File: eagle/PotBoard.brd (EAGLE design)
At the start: 62 x 29 mm, 29 parts, among them IC1 MEGA8-AI, Q1 20MHz, Q3 IRLML5203, X1 MICROMATCH-8SMD

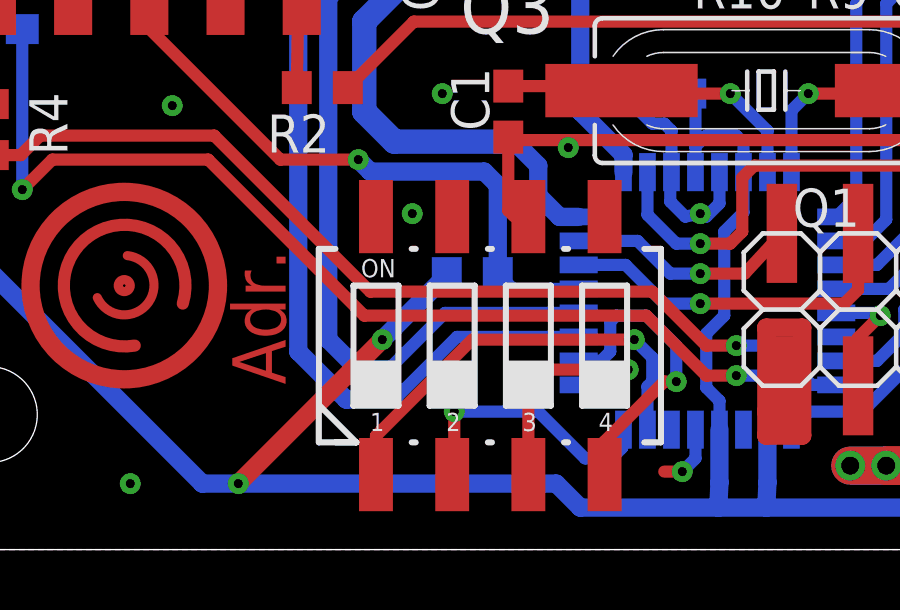
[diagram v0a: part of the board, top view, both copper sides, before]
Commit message: Removed a stupid error from the pcbs and included an instructions file. Switched the firmware to use just two switches instead of four. No one's gonna build an arc16 anyway.
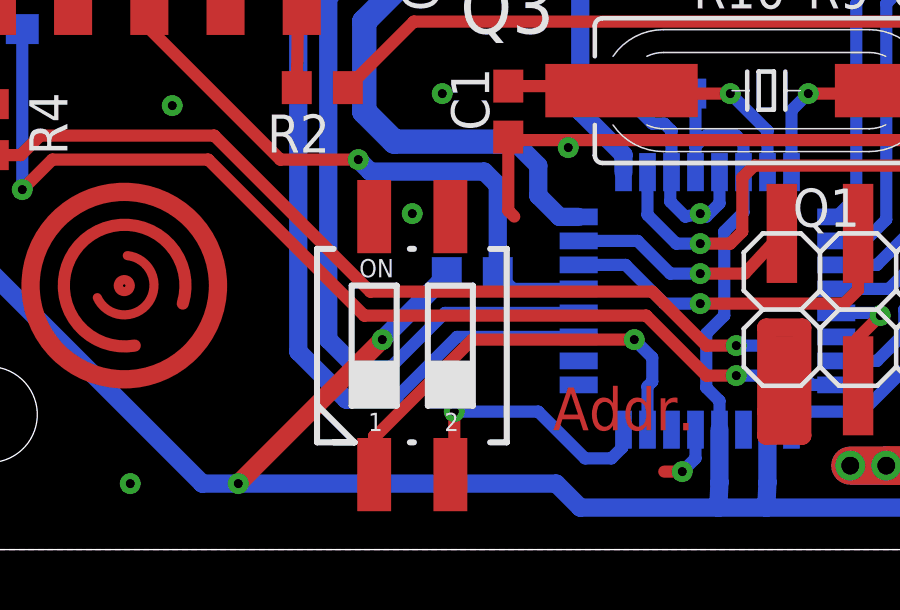
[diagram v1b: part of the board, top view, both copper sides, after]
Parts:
- removed S1: 219-04, switch-dil:CTS-219-04
- added ADRESS: 219-02, switch-dil:CTS-219-02
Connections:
- removed net N$22: IC1.25, S1.3
- removed net N$23: IC1.26, S1.4
- net GND: now also ADRESS.3, ADRESS.4; no longer S1.5, S1.6, S1.7, S1.8
- net N$20: now also ADRESS.2; no longer S1.2
- net N$6: now also ADRESS.1; no longer S1.1
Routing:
- net N$23: track 10.4 -> 0.00 mm, vias 1 -> 0
- net N$22: track 8.27 -> 0.00 mm, vias 1 -> 0
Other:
- board text added: "Addr."
- board text removed: "Adr."
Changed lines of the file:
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@@
 <layer number="17" name="Pads" color="2" fill="1" visible="yes" active="yes"/>
 <layer number="18" name="Vias" color="2" fill="1" visible="yes" active="yes"/>
-<layer number="19" name="Unrouted" color="6" fill="1" visible="no" active="yes"/>
+<layer number="19" name="Unrouted" color="6" fill="1" visible="yes" active="yes"/>
 <layer number="20" name="Dimension" color="15" fill="1" visible="yes" active="yes"/>
 <layer number="21" name="tPlace" color="7" fill="1" visible="yes" active="yes"/>
 <layer number="22" name="bPlace" color="7" fill="1" visible="no" active="yes"/>
-<layer number="23" name="tOrigins" color="15" fill="1" visible="no" active="yes"/>
+<layer number="23" name="tOrigins" color="15" fill="1" visible="yes" active="yes"/>
 <layer number="24" name="bOrigins" color="15" fill="1" visible="no" active="yes"/>
 <layer number="25" name="tNames" color="7" fill="1" visible="yes" active="yes"/>
@@
 <circle x="9" y="8.8" radius="0.2" width="0.3048" layer="1"/>
 <text x="60.6" y="7" size="2.54" layer="1" font="vector" ratio="16" rot="R90">Arc_Base</text>
-<text x="12.6" y="10" size="1.778" layer="1" font="vector" ratio="15" rot="R270">Adr.</text>
+<text x="28" y="5.4" size="1.4224" layer="1" font="vector" ratio="15" rot="R180">Addr.</text>
 <text x="42.2" y="26.6" size="1.27" layer="1" font="vector" ratio="17">Johannes Neumann</text>
 <text x="61" y="25.2" size="2.54" layer="16" font="vector" ratio="16" rot="MR270">Arc_Base</text>
@@
 <attribute name="VALUE" x="29.65" y="3.555" size="1.27" layer="27"/>
 </element>
-<element name="S1" library="switch-dil" package="CTS-219-04" value="219-04" x="21.2" y="6.8" smashed="yes">
-<attribute name="OC_NEWARK" value="unknown" x="21.2" y="6.8" size="1.27" layer="27" font="vector" ratio="17" display="off"/>
-<attribute name="MPN" value="" x="21.2" y="6.8" size="1.27" layer="27" font="vector" ratio="17" display="off"/>
-<attribute name="MF" value="" x="21.2" y="6.8" size="1.27" layer="27" font="vector" ratio="17" display="off"/>
-<attribute name="OC_FARNELL" value="unknown" x="21.2" y="6.8" size="1.27" layer="27" font="vector" ratio="17" display="off"/>
-</element>
 <element name="R2" library="rcl" package="R0603" value="330" x="15.6" y="15.4" smashed="yes">
 <attribute name="NAME" x="13.765" y="13.235" size="1.27" layer="25"/>
@@
 <element name="X1" library="con-amp-micromatch-2" package="MICROMATCH-8-SMD" value="MICROMATCH-8SMD" x="49.4" y="21.6" smashed="yes" rot="R180">
 <attribute name="NAME" x="55.045" y="18.66" size="1.27" layer="25" rot="R180"/>
+</element>
+<element name="ADRESS" library="switch-dil" package="CTS-219-02" value="219-02" x="18.6" y="6.8" smashed="yes">
+<attribute name="OC_NEWARK" value="unknown" x="18.6" y="6.8" size="1.778" layer="27" display="off"/>
+<attribute name="MPN" value="" x="18.6" y="6.8" size="1.778" layer="27" display="off"/>
+<attribute name="MF" value="" x="18.6" y="6.8" size="1.778" layer="27" display="off"/>
+<attribute name="OC_FARNELL" value="unknown" x="18.6" y="6.8" size="1.778" layer="27" display="off"/>
 </element>
 </elements>
@@
 <via x="2.4" y="8.8" extent="1-16" drill="0.3" shape="octagon"/>
 <via x="39.8" y="7.8" extent="1-16" drill="0.3" shape="octagon"/>
-<contactref element="S1" pad="5"/>
-<contactref element="S1" pad="6"/>
-<contactref element="S1" pad="7"/>
-<contactref element="S1" pad="8"/>
 <via x="38.6" y="25.8" extent="1-16" drill="0.3" shape="octagon"/>
 <via x="49.6" y="12.8" extent="1-16" drill="0.3" shape="octagon"/>
@@
 <wire x1="30.92" y1="5.46" x2="30.92" y2="5.12" width="0.6096" layer="1"/>
 <wire x1="30.92" y1="5.12" x2="30.4" y2="4.6" width="0.6096" layer="1"/>
+<contactref element="ADRESS" pad="3"/>
+<contactref element="ADRESS" pad="4"/>
 </signal>
 <signal name="VCC">
@@
 <wire x1="26.6" y1="6.4" x2="26" y2="7" width="0.4064" layer="16"/>
 <wire x1="26" y1="7" x2="20.6" y2="7" width="0.4064" layer="1"/>
-<contactref element="S1" pad="1"/>
-<wire x1="17.39" y1="2.5" x2="17.39" y2="3.79" width="0.4064" layer="1"/>
+<contactref element="ADRESS" pad="1"/>
+<wire x1="17.39" y1="3.79" x2="17.33" y2="3.79" width="0.4064" layer="1"/>
+<wire x1="17.33" y1="3.79" x2="17.33" y2="2.5" width="0.4064" layer="1"/>
 </signal>
 <signal name="N$20">
@@
 <wire x1="24.36" y1="3.04" x2="22.8" y2="4.6" width="0.4064" layer="16"/>
 <wire x1="22.8" y1="4.6" x2="20" y2="4.6" width="0.4064" layer="16"/>
-<contactref element="S1" pad="2"/>
 <wire x1="20" y1="4.6" x2="20" y2="2.57" width="0.4064" layer="1"/>
-<wire x1="20" y1="2.57" x2="19.93" y2="2.5" width="0.4064" layer="1"/>
-</signal>
-<signal name="N$22">
-<contactref element="IC1" pad="25"/>
-<via x="25.8" y="6" extent="1-16" drill="0.3" shape="octagon"/>
-<wire x1="24.1474" y1="5.49" x2="25.29" y2="5.49" width="0.4064" layer="16"/>
-<wire x1="25.29" y1="5.49" x2="25.8" y2="6" width="0.4064" layer="16"/>
-<contactref element="S1" pad="3"/>
-<wire x1="22.47" y1="2.5" x2="22.47" y2="5.27" width="0.4064" layer="1"/>
-<wire x1="22.47" y1="5.27" x2="23.2" y2="6" width="0.4064" layer="1"/>
-<wire x1="23.2" y1="6" x2="25.8" y2="6" width="0.4064" layer="1"/>
-</signal>
-<signal name="N$23">
-<contactref element="IC1" pad="26"/>
-<via x="27.4" y="5.6" extent="1-16" drill="0.3" shape="octagon"/>
-<wire x1="24.1474" y1="6.29" x2="24.89" y2="6.29" width="0.4064" layer="16"/>
-<wire x1="24.89" y1="6.29" x2="25.2" y2="6.6" width="0.4064" layer="16"/>
-<wire x1="25.2" y1="6.6" x2="25.2" y2="7.6" width="0.4064" layer="16"/>
-<wire x1="25.2" y1="7.6" x2="25.4" y2="7.8" width="0.4064" layer="16"/>
-<wire x1="25.4" y1="7.8" x2="26.4" y2="7.8" width="0.4064" layer="16"/>
-<wire x1="26.4" y1="7.8" x2="27.4" y2="6.8" width="0.4064" layer="16"/>
-<wire x1="27.4" y1="6.8" x2="27.4" y2="5.6" width="0.4064" layer="16"/>
-<contactref element="S1" pad="4"/>
-<wire x1="27.4" y1="5.6" x2="27" y2="5.6" width="0.4064" layer="1"/>
-<wire x1="27" y1="5.6" x2="25" y2="3.6" width="0.4064" layer="1"/>
-<wire x1="25" y1="3.6" x2="25" y2="2.51" width="0.4064" layer="1"/>
-<wire x1="25" y1="2.51" x2="25.01" y2="2.5" width="0.4064" layer="1"/>
+<contactref element="ADRESS" pad="2"/>
+<wire x1="20" y1="2.57" x2="19.87" y2="2.57" width="0.4064" layer="1"/>
+<wire x1="19.87" y1="2.57" x2="19.87" y2="2.5" width="0.4064" layer="1"/>
 </signal>
 <signal name="N$26">
